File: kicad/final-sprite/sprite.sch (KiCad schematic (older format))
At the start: 64 parts, among them J1 M20-7910442R, U1 CC430F513X, U2 LSM9DS1, U3 SPRITETCXO_TCXO_7Z, U4 DRV8837, U5 ADP5092, U6 DRV8837, U7 DRV8837, X1 SPRITEPIN_SPRITE_PIN, X2 SPRITEPIN_SPRITE_PIN

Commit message: Save supercap footprint in sprite library
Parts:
- C10: footprint CAPCP3225X100N -> sprite:CAPCP3225X100N; symbol CPH3225A:CPH3225A -> sprite-rescue:CPH3225A-CPH3225A
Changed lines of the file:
@@
 ~RST
 $Comp
-L CPH3225A:CPH3225A C10
+L sprite-rescue:CPH3225A-CPH3225A C10
 U 1 1 5B82E146
 P 11700 3850
 F 0 "C10" H 11830 3846 50  0000 L CNN
 F 1 "CPH3225A" H 11830 3755 50  0000 L CNN
-F 2 "CAPCP3225X100N" H 11700 3850 50  0001 L BNN
+F 2 "sprite:CAPCP3225X100N" H 11700 3850 50  0001 L BNN
 F 3 "Seiko" H 11700 3850 50  0001 L BNN
 F 4 "1210 Seiko" H 11700 3850 50  0001 L BNN "Field4"

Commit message: Dump in a few more supercaps
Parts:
- added C18, C19, C20, C21, C22: CPH3225A, sprite:CAPCP3225X100N, symbol sprite-rescue:CPH3225A-CPH3225A
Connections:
- wire segments 268 -> 273
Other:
- moved on the sheet: C10
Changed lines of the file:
@@
 Wire Notes Line
 	7100 550  7100 10450
-Wire Notes Line
-	800  4550 15700 4550
 $Comp
 L sprite-rescue:Mounting_Hole-Mechanical MK1
@@
 ~RST
 $Comp
+L sprite-eagle-import:GND #GND0101
+U 1 0 5B85E9B2
+P 11700 4300
+F 0 "#GND0101" H 11700 4300 50  0001 C CNN
+F 1 "GND" H 11600 4200 59  0000 L BNN
+F 2 "" H 11700 4300 50  0001 C CNN
+F 3 "" H 11700 4300 50  0001 C CNN
+	1    11700 4300
+	1    0    0    -1
+$EndComp
+$Comp
 L sprite-rescue:CPH3225A-CPH3225A C10
 U 1 1 5B82E146
-P 11700 3850
-F 0 "C10" H 11830 3846 50  0000 L CNN
-F 1 "CPH3225A" H 11830 3755 50  0000 L CNN
-F 2 "sprite:CAPCP3225X100N" H 11700 3850 50  0001 L BNN
-F 3 "Seiko" H 11700 3850 50  0001 L BNN
-F 4 "1210 Seiko" H 11700 3850 50  0001 L BNN "Field4"
-F 5 "https://www.digikey.com/product-detail/en/seiko-instruments/CPH3225A/728-1127-1-ND/8692445?utm_source=snapeda&utm_medium=aggregator&utm_campaign=symbol" H 11700 3850 50  0001 L BNN "Field5"
-F 6 "728-1127-1-ND" H 11700 3850 50  0001 L BNN "Field6"
-F 7 "Cap 11mf 3.3v Surface Mount" H 11700 3850 50  0001 L BNN "Field7"
-F 8 "CPH3225A" H 11700 3850 50  0001 L BNN "Field8"
-	1    11700 3850
-	1    0    0    -1
-$EndComp
+P 11700 3800
+F 0 "C10" H 11830 3796 50  0000 L CNN
+F 1 "CPH3225A" H 11830 3705 50  0000 L CNN
+F 2 "sprite:CAPCP3225X100N" H 11700 3800 50  0001 L BNN
+F 3 "Seiko" H 11700 3800 50  0001 L BNN
+F 4 "1210 Seiko" H 11700 3800 50  0001 L BNN "Field4"
+F 5 "https://www.digikey.com/product-detail/en/seiko-instruments/CPH3225A/728-1127-1-ND/8692445?utm_source=snapeda&utm_medium=aggregator&utm_campaign=symbol" H 11700 3800 50  0001 L BNN "Field5"
+F 6 "728-1127-1-ND" H 11700 3800 50  0001 L BNN "Field6"
+F 7 "Cap 11mf 3.3v Surface Mount" H 11700 3800 50  0001 L BNN "Field7"
+F 8 "CPH3225A" H 11700 3800 50  0001 L BNN "Field8"
+	1    11700 3800
+	1    0    0    -1
+$EndComp
+$Comp
+L sprite-eagle-import:GND #GND0102
+U 1 0 5B89C81E
+P 12400 4300
+F 0 "#GND0102" H 12400 4300 50  0001 C CNN
+F 1 "GND" H 12300 4200 59  0000 L BNN
+F 2 "" H 12400 4300 50  0001 C CNN
+F 3 "" H 12400 4300 50  0001 C CNN
+	1    12400 4300
+	1    0    0    -1
+$EndComp
+$Comp
+L sprite-rescue:CPH3225A-CPH3225A C18
+U 1 1 5B89C829
+P 12400 3800
+F 0 "C18" H 12530 3796 50  0000 L CNN
+F 1 "CPH3225A" H 12530 3705 50  0000 L CNN
+F 2 "sprite:CAPCP3225X100N" H 12400 3800 50  0001 L BNN
+F 3 "Seiko" H 12400 3800 50  0001 L BNN
+F 4 "1210 Seiko" H 12400 3800 50  0001 L BNN "Field4"
+F 5 "https://www.digikey.com/product-detail/en/seiko-instruments/CPH3225A/728-1127-1-ND/8692445?utm_source=snapeda&utm_medium=aggregator&utm_campaign=symbol" H 12400 3800 50  0001 L BNN "Field5"
+F 6 "728-1127-1-ND" H 12400 3800 50  0001 L BNN "Field6"
+F 7 "Cap 11mf 3.3v Surface Mount" H 12400 3800 50  0001 L BNN "Field7"
+F 8 "CPH3225A" H 12400 3800 50  0001 L BNN "Field8"
+	1    12400 3800
+	1    0    0    -1
+$EndComp
+$Comp
+L sprite-eagle-import:GND #GND0103
+U 1 0 5B8C5C56
+P 13100 4300
+F 0 "#GND0103" H 13100 4300 50  0001 C CNN
+F 1 "GND" H 13000 4200 59  0000 L BNN
+F 2 "" H 13100 4300 50  0001 C CNN
+F 3 "" H 13100 4300 50  0001 C CNN
+	1    13100 4300
+	1    0    0    -1
+$EndComp
+$Comp
+L sprite-rescue:CPH3225A-CPH3225A C19
+U 1 1 5B8C5C61
+P 13100 3800
+F 0 "C19" H 13230 3796 50  0000 L CNN
+F 1 "CPH3225A" H 13230 3705 50  0000 L CNN
+F 2 "sprite:CAPCP3225X100N" H 13100 3800 50  0001 L BNN
+F 3 "Seiko" H 13100 3800 50  0001 L BNN
+F 4 "1210 Seiko" H 13100 3800 50  0001 L BNN "Field4"
+F 5 "https://www.digikey.com/product-detail/en/seiko-instruments/CPH3225A/728-1127-1-ND/8692445?utm_source=snapeda&utm_medium=aggregator&utm_campaign=symbol" H 13100 3800 50  0001 L BNN "Field5"
+F 6 "728-1127-1-ND" H 13100 3800 50  0001 L BNN "Field6"
+F 7 "Cap 11mf 3.3v Surface Mount" H 13100 3800 50  0001 L BNN "Field7"
+F 8 "CPH3225A" H 13100 3800 50  0001 L BNN "Field8"
+	1    13100 3800
+	1    0    0    -1
+$EndComp
+Wire Wire Line
+	11700 3500 12400 3500
+Connection ~ 12400 3500
+Wire Wire Line
+	12400 3500 13100 3500
+Text Label 11950 3500 0    50   ~ 0
+VBAT
+$Comp
+L sprite-eagle-import:GND #GND0104
+U 1 0 5B91904C
+P 13800 4300
+F 0 "#GND0104" H 13800 4300 50  0001 C CNN
+F 1 "GND" H 13700 4200 59  0000 L BNN
+F 2 "" H 13800 4300 50  0001 C CNN
+F 3 "" H 13800 4300 50  0001 C CNN
+	1    13800 4300
+	1    0    0    -1
+$EndComp
+$Comp
+L sprite-rescue:CPH3225A-CPH3225A C20
+U 1 1 5B919057
+P 13800 3800
+F 0 "C20" H 13930 3796 50  0000 L CNN
+F 1 "CPH3225A" H 13930 3705 50  0000 L CNN
+F 2 "sprite:CAPCP3225X100N" H 13800 3800 50  0001 L BNN
+F 3 "Seiko" H 13800 3800 50  0001 L BNN
+F 4 "1210 Seiko" H 13800 3800 50  0001 L BNN "Field4"
+F 5 "https://www.digikey.com/product-detail/en/seiko-instruments/CPH3225A/728-1127-1-ND/8692445?utm_source=snapeda&utm_medium=aggregator&utm_campaign=symbol" H 13800 3800 50  0001 L BNN "Field5"
+F 6 "728-1127-1-ND" H 13800 3800 50  0001 L BNN "Field6"
+F 7 "Cap 11mf 3.3v Surface Mount" H 13800 3800 50  0001 L BNN "Field7"
+F 8 "CPH3225A" H 13800 3800 50  0001 L BNN "Field8"
+	1    13800 3800
+	1    0    0    -1
+$EndComp
+$Comp
+L sprite-eagle-import:GND #GND0105
+U 1 0 5B91905D
+P 14500 4300
+F 0 "#GND0105" H 14500 4300 50  0001 C CNN
+F 1 "GND" H 14400 4200 59  0000 L BNN
+F 2 "" H 14500 4300 50  0001 C CNN
+F 3 "" H 14500 4300 50  0001 C CNN
+	1    14500 4300
+	1    0    0    -1
+$EndComp
+$Comp
+L sprite-rescue:CPH3225A-CPH3225A C21
+U 1 1 5B919068
+P 14500 3800
+F 0 "C21" H 14630 3796 50  0000 L CNN
+F 1 "CPH3225A" H 14630 3705 50  0000 L CNN
+F 2 "sprite:CAPCP3225X100N" H 14500 3800 50  0001 L BNN
+F 3 "Seiko" H 14500 3800 50  0001 L BNN
+F 4 "1210 Seiko" H 14500 3800 50  0001 L BNN "Field4"
+F 5 "https://www.digikey.com/product-detail/en/seiko-instruments/CPH3225A/728-1127-1-ND/8692445?utm_source=snapeda&utm_medium=aggregator&utm_campaign=symbol" H 14500 3800 50  0001 L BNN "Field5"
+F 6 "728-1127-1-ND" H 14500 3800 50  0001 L BNN "Field6"
+F 7 "Cap 11mf 3.3v Surface Mount" H 14500 3800 50  0001 L BNN "Field7"
+F 8 "CPH3225A" H 14500 3800 50  0001 L BNN "Field8"
+	1    14500 3800
+	1    0    0    -1
+$EndComp
+$Comp
+L sprite-eagle-import:GND #GND0106
+U 1 0 5B91906E
+P 15200 4300
+F 0 "#GND0106" H 15200 4300 50  0001 C CNN
+F 1 "GND" H 15100 4200 59  0000 L BNN
+F 2 "" H 15200 4300 50  0001 C CNN
+F 3 "" H 15200 4300 50  0001 C CNN
+	1    15200 4300
+	1    0    0    -1
+$EndComp
+$Comp
+L sprite-rescue:CPH3225A-CPH3225A C22
+U 1 1 5B919079
+P 15200 3800
+F 0 "C22" H 15330 3796 50  0000 L CNN
+F 1 "CPH3225A" H 15330 3705 50  0000 L CNN
+F 2 "sprite:CAPCP3225X100N" H 15200 3800 50  0001 L BNN
+F 3 "Seiko" H 15200 3800 50  0001 L BNN
+F 4 "1210 Seiko" H 15200 3800 50  0001 L BNN "Field4"
+F 5 "https://www.digikey.com/product-detail/en/seiko-instruments/CPH3225A/728-1127-1-ND/8692445?utm_source=snapeda&utm_medium=aggregator&utm_campaign=symbol" H 15200 3800 50  0001 L BNN "Field5"
+F 6 "728-1127-1-ND" H 15200 3800 50  0001 L BNN "Field6"
+F 7 "Cap 11mf 3.3v Surface Mount" H 15200 3800 50  0001 L BNN "Field7"
+F 8 "CPH3225A" H 15200 3800 50  0001 L BNN "Field8"
+	1    15200 3800
+	1    0    0    -1
+$EndComp
+Wire Wire Line
+	13800 3500 14500 3500
+Connection ~ 14500 3500
+Wire Wire Line
+	14500 3500 15200 3500
+Wire Wire Line
+	13800 3500 13100 3500
+Connection ~ 13800 3500
+Connection ~ 13100 3500
 $EndSCHEMATC

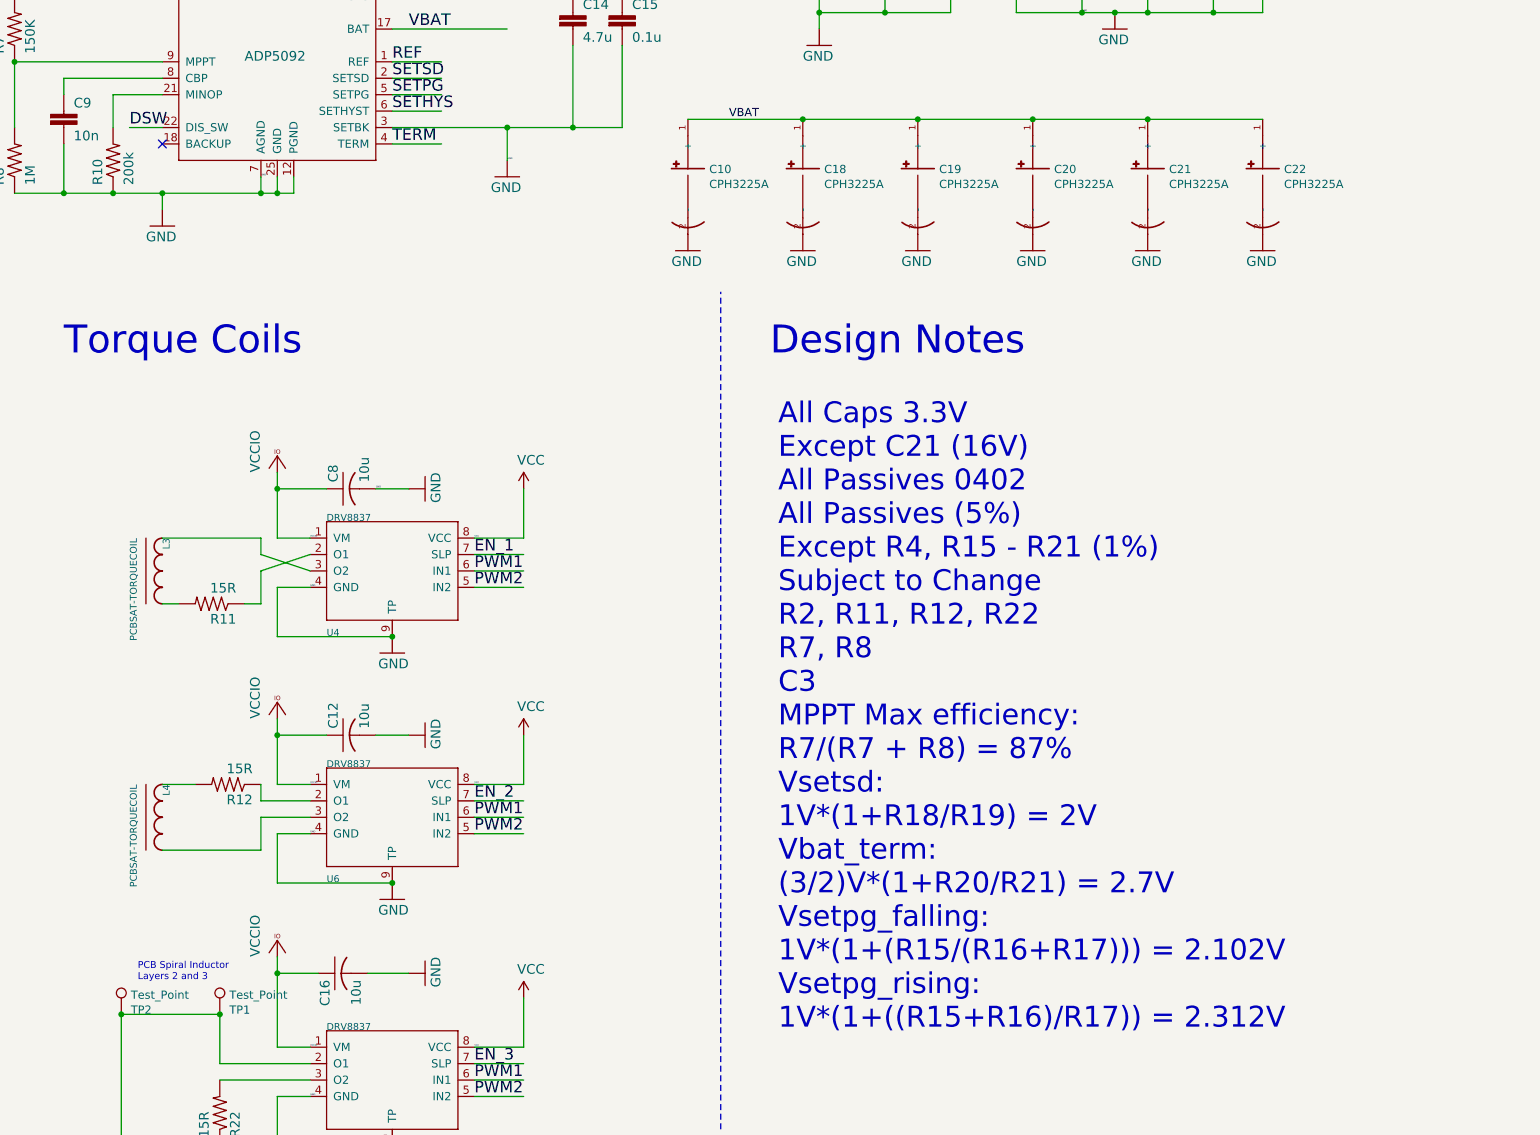
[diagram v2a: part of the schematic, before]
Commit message: added more caps and moved a couple traces
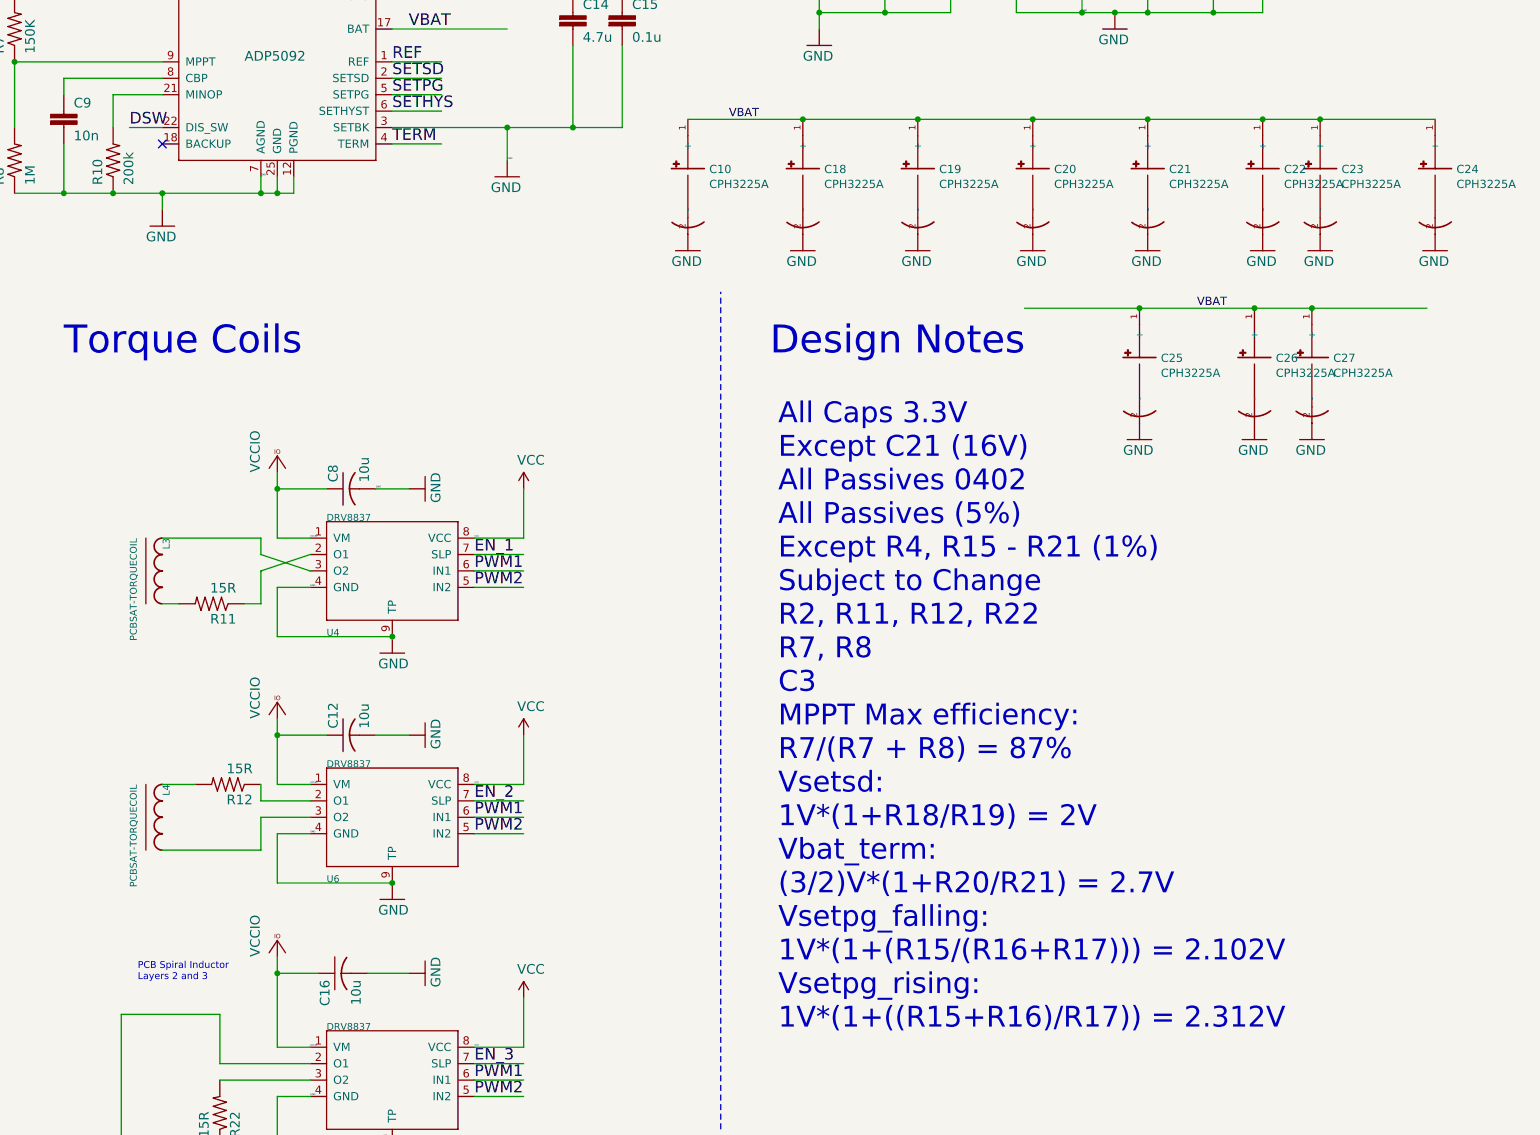
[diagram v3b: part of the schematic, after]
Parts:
- removed TP1, TP2: Test_Point, TestPoint:TestPoint_Pad_D1.0mm, symbol sprite-rescue:Test_Point-Connector
- added C23, C24, C25, C26, C27: CPH3225A, sprite:CAPCP3225X100N, symbol sprite-rescue:CPH3225A-CPH3225A
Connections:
- wire segments 273 -> 279
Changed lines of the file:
@@
 Wire Wire Line
 	9750 8700 10000 8700
-$Comp
-L sprite-rescue:Test_Point-Connector TP2
-U 1 1 5B335398
-P 8250 8950
-F 0 "TP2" H 8192 8977 50  0000 R CNN
-F 1 "Test_Point" H 8192 9068 50  0000 R CNN
-F 2 "TestPoint:TestPoint_Pad_D1.0mm" H 8450 8950 50  0001 C CNN
-F 3 "~" H 8450 8950 50  0001 C CNN
-	1    8250 8950
-	-1   0    0    -1
-$EndComp
 Wire Wire Line
 	8850 9750 8250 9750
@@
 Wire Wire Line
 	8850 8950 8850 9250
-Connection ~ 8250 8950
 Wire Wire Line
 	8850 9250 9400 9250
@@
 NoConn ~ 4700 2850
 $Comp
-L sprite-rescue:Test_Point-Connector TP1
-U 1 1 5B3A87A5
-P 8850 8950
-F 0 "TP1" H 8792 8977 50  0000 R CNN
-F 1 "Test_Point" H 8792 9068 50  0000 R CNN
-F 2 "TestPoint:TestPoint_Pad_D1.0mm" H 9050 8950 50  0001 C CNN
-F 3 "~" H 9050 8950 50  0001 C CNN
-	1    8850 8950
-	-1   0    0    -1
-$EndComp
-Connection ~ 8850 8950
-$Comp
 L sprite-eagle-import:R-US_R0402 R23
 U 1 0 5B3C09A9
@@
 Wire Wire Line
 	13800 3500 14500 3500
-Connection ~ 14500 3500
 Wire Wire Line
 	14500 3500 15200 3500
@@
 Connection ~ 13800 3500
 Connection ~ 13100 3500
+Connection ~ 14500 3500
+$Comp
+L sprite-eagle-import:GND #GND0107
+U 1 0 5B823DAB
+P 15550 4300
+F 0 "#GND0107" H 15550 4300 50  0001 C CNN
+F 1 "GND" H 15450 4200 59  0000 L BNN
+F 2 "" H 15550 4300 50  0001 C CNN
+F 3 "" H 15550 4300 50  0001 C CNN
+	1    15550 4300
+	1    0    0    -1
+$EndComp
+$Comp
+L sprite-rescue:CPH3225A-CPH3225A C23
+U 1 1 5B823DB6
+P 15550 3800
+F 0 "C23" H 15680 3796 50  0000 L CNN
+F 1 "CPH3225A" H 15680 3705 50  0000 L CNN
+F 2 "sprite:CAPCP3225X100N" H 15550 3800 50  0001 L BNN
+F 3 "Seiko" H 15550 3800 50  0001 L BNN
+F 4 "1210 Seiko" H 15550 3800 50  0001 L BNN "Field4"
+F 5 "https://www.digikey.com/product-detail/en/seiko-instruments/CPH3225A/728-1127-1-ND/8692445?utm_source=snapeda&utm_medium=aggregator&utm_campaign=symbol" H 15550 3800 50  0001 L BNN "Field5"
+F 6 "728-1127-1-ND" H 15550 3800 50  0001 L BNN "Field6"
+F 7 "Cap 11mf 3.3v Surface Mount" H 15550 3800 50  0001 L BNN "Field7"
+F 8 "CPH3225A" H 15550 3800 50  0001 L BNN "Field8"
+	1    15550 3800
+	1    0    0    -1
+$EndComp
+$Comp
+L sprite-eagle-import:GND #GND0108
+U 1 0 5B823DBC
+P 16250 4300
+F 0 "#GND0108" H 16250 4300 50  0001 C CNN
+F 1 "GND" H 16150 4200 59  0000 L BNN
+F 2 "" H 16250 4300 50  0001 C CNN
+F 3 "" H 16250 4300 50  0001 C CNN
+	1    16250 4300
+	1    0    0    -1
+$EndComp
+$Comp
+L sprite-rescue:CPH3225A-CPH3225A C24
+U 1 1 5B823DC7
+P 16250 3800
+F 0 "C24" H 16380 3796 50  0000 L CNN
+F 1 "CPH3225A" H 16380 3705 50  0000 L CNN
+F 2 "sprite:CAPCP3225X100N" H 16250 3800 50  0001 L BNN
+F 3 "Seiko" H 16250 3800 50  0001 L BNN
+F 4 "1210 Seiko" H 16250 3800 50  0001 L BNN "Field4"
+F 5 "https://www.digikey.com/product-detail/en/seiko-instruments/CPH3225A/728-1127-1-ND/8692445?utm_source=snapeda&utm_medium=aggregator&utm_campaign=symbol" H 16250 3800 50  0001 L BNN "Field5"
+F 6 "728-1127-1-ND" H 16250 3800 50  0001 L BNN "Field6"
+F 7 "Cap 11mf 3.3v Surface Mount" H 16250 3800 50  0001 L BNN "Field7"
+F 8 "CPH3225A" H 16250 3800 50  0001 L BNN "Field8"
+	1    16250 3800
+	1    0    0    -1
+$EndComp
+Wire Wire Line
+	15550 3500 16250 3500
+Connection ~ 15550 3500
+Wire Wire Line
+	15200 3500 15550 3500
+Connection ~ 15200 3500
+$Comp
+L sprite-eagle-import:GND #GND0109
+U 1 0 5B892CAD
+P 14450 5450
+F 0 "#GND0109" H 14450 5450 50  0001 C CNN
+F 1 "GND" H 14350 5350 59  0000 L BNN
+F 2 "" H 14450 5450 50  0001 C CNN
+F 3 "" H 14450 5450 50  0001 C CNN
+	1    14450 5450
+	1    0    0    -1
+$EndComp
+$Comp
+L sprite-rescue:CPH3225A-CPH3225A C25
+U 1 1 5B892CB8
+P 14450 4950
+F 0 "C25" H 14580 4946 50  0000 L CNN
+F 1 "CPH3225A" H 14580 4855 50  0000 L CNN
+F 2 "sprite:CAPCP3225X100N" H 14450 4950 50  0001 L BNN
+F 3 "Seiko" H 14450 4950 50  0001 L BNN
+F 4 "1210 Seiko" H 14450 4950 50  0001 L BNN "Field4"
+F 5 "https://www.digikey.com/product-detail/en/seiko-instruments/CPH3225A/728-1127-1-ND/8692445?utm_source=snapeda&utm_medium=aggregator&utm_campaign=symbol" H 14450 4950 50  0001 L BNN "Field5"
+F 6 "728-1127-1-ND" H 14450 4950 50  0001 L BNN "Field6"
+F 7 "Cap 11mf 3.3v Surface Mount" H 14450 4950 50  0001 L BNN "Field7"
+F 8 "CPH3225A" H 14450 4950 50  0001 L BNN "Field8"
+	1    14450 4950
+	1    0    0    -1
+$EndComp
+$Comp
+L sprite-eagle-import:GND #GND0110
+U 1 0 5B892CBE
+P 15150 5450
+F 0 "#GND0110" H 15150 5450 50  0001 C CNN
+F 1 "GND" H 15050 5350 59  0000 L BNN
+F 2 "" H 15150 5450 50  0001 C CNN
+F 3 "" H 15150 5450 50  0001 C CNN
+	1    15150 5450
+	1    0    0    -1
+$EndComp
+$Comp
+L sprite-rescue:CPH3225A-CPH3225A C26
+U 1 1 5B892CC9
+P 15150 4950
+F 0 "C26" H 15280 4946 50  0000 L CNN
+F 1 "CPH3225A" H 15280 4855 50  0000 L CNN
+F 2 "sprite:CAPCP3225X100N" H 15150 4950 50  0001 L BNN
+F 3 "Seiko" H 15150 4950 50  0001 L BNN
+F 4 "1210 Seiko" H 15150 4950 50  0001 L BNN "Field4"
+F 5 "https://www.digikey.com/product-detail/en/seiko-instruments/CPH3225A/728-1127-1-ND/8692445?utm_source=snapeda&utm_medium=aggregator&utm_campaign=symbol" H 15150 4950 50  0001 L BNN "Field5"
+F 6 "728-1127-1-ND" H 15150 4950 50  0001 L BNN "Field6"
+F 7 "Cap 11mf 3.3v Surface Mount" H 15150 4950 50  0001 L BNN "Field7"
+F 8 "CPH3225A" H 15150 4950 50  0001 L BNN "Field8"
+	1    15150 4950
+	1    0    0    -1
+$EndComp
+Wire Wire Line
+	13750 4650 14450 4650
+Wire Wire Line
+	14450 4650 15150 4650
+Connection ~ 14450 4650
+$Comp
+L sprite-eagle-import:GND #GND0111
+U 1 0 5B892CD2
+P 15500 5450
+F 0 "#GND0111" H 15500 5450 50  0001 C CNN
+F 1 "GND" H 15400 5350 59  0000 L BNN
+F 2 "" H 15500 5450 50  0001 C CNN
+F 3 "" H 15500 5450 50  0001 C CNN
+	1    15500 5450
+	1    0    0    -1
+$EndComp
+$Comp
+L sprite-rescue:CPH3225A-CPH3225A C27
+U 1 1 5B892CDD
+P 15500 4950
+F 0 "C27" H 15630 4946 50  0000 L CNN
+F 1 "CPH3225A" H 15630 4855 50  0000 L CNN
+F 2 "sprite:CAPCP3225X100N" H 15500 4950 50  0001 L BNN
+F 3 "Seiko" H 15500 4950 50  0001 L BNN
+F 4 "1210 Seiko" H 15500 4950 50  0001 L BNN "Field4"
+F 5 "https://www.digikey.com/product-detail/en/seiko-instruments/CPH3225A/728-1127-1-ND/8692445?utm_source=snapeda&utm_medium=aggregator&utm_campaign=symbol" H 15500 4950 50  0001 L BNN "Field5"
+F 6 "728-1127-1-ND" H 15500 4950 50  0001 L BNN "Field6"
+F 7 "Cap 11mf 3.3v Surface Mount" H 15500 4950 50  0001 L BNN "Field7"
+F 8 "CPH3225A" H 15500 4950 50  0001 L BNN "Field8"
+	1    15500 4950
+	1    0    0    -1
+$EndComp
+Wire Wire Line
+	15500 4650 16200 4650
+Connection ~ 15500 4650
+Wire Wire Line
+	15150 4650 15500 4650
+Connection ~ 15150 4650
+Text Label 14800 4650 0    50   ~ 0
+VBAT
 $EndSCHEMATC
